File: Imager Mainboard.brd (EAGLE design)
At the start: 63.5 x 65 mm, 45 parts, among them IC1 7805H, IC2 MAX3490, IC3 SC16IS740IPW, IC4 MAX3490, IC6 AD7714R-24, J1 RASPBERRYPI-40-PIN-GPIO_PTH_N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, J14 U.FL, Q1 ASFL1, Q2 1.8432 MHz

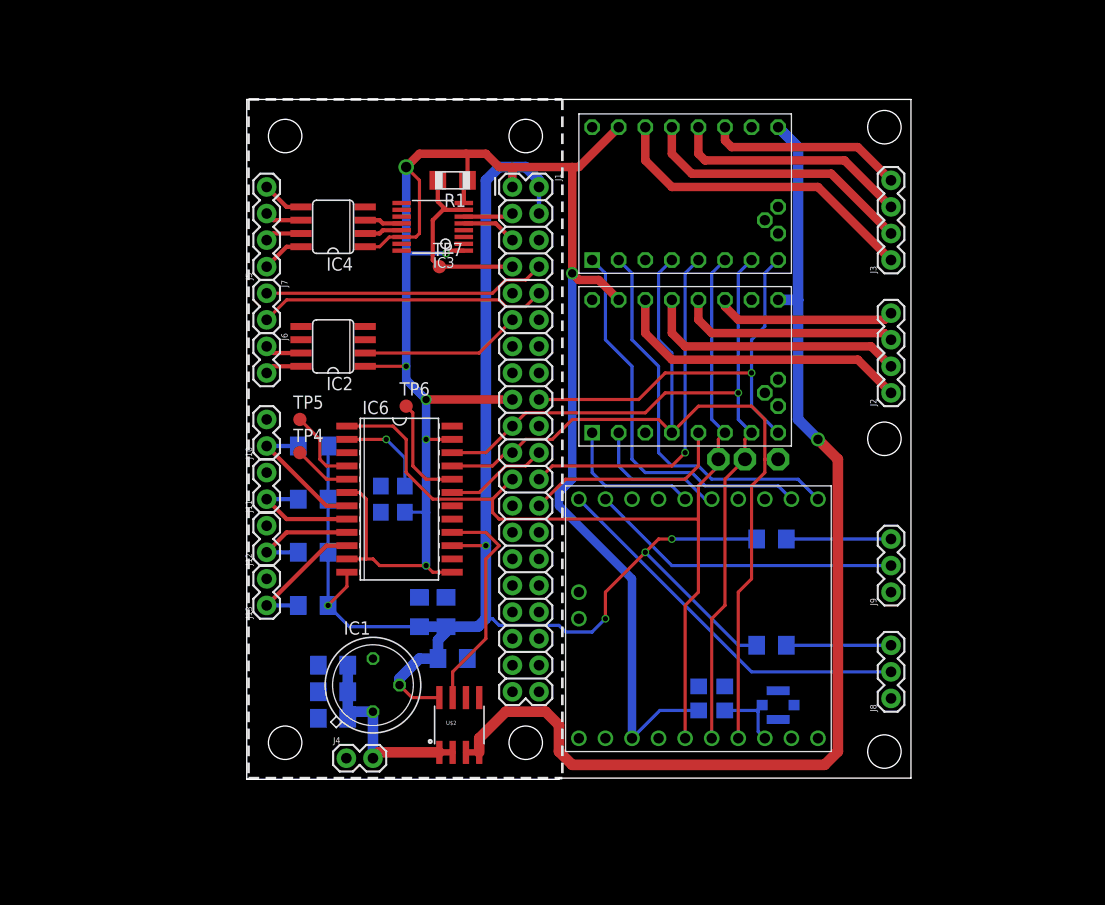
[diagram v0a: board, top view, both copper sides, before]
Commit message: Adding test pads
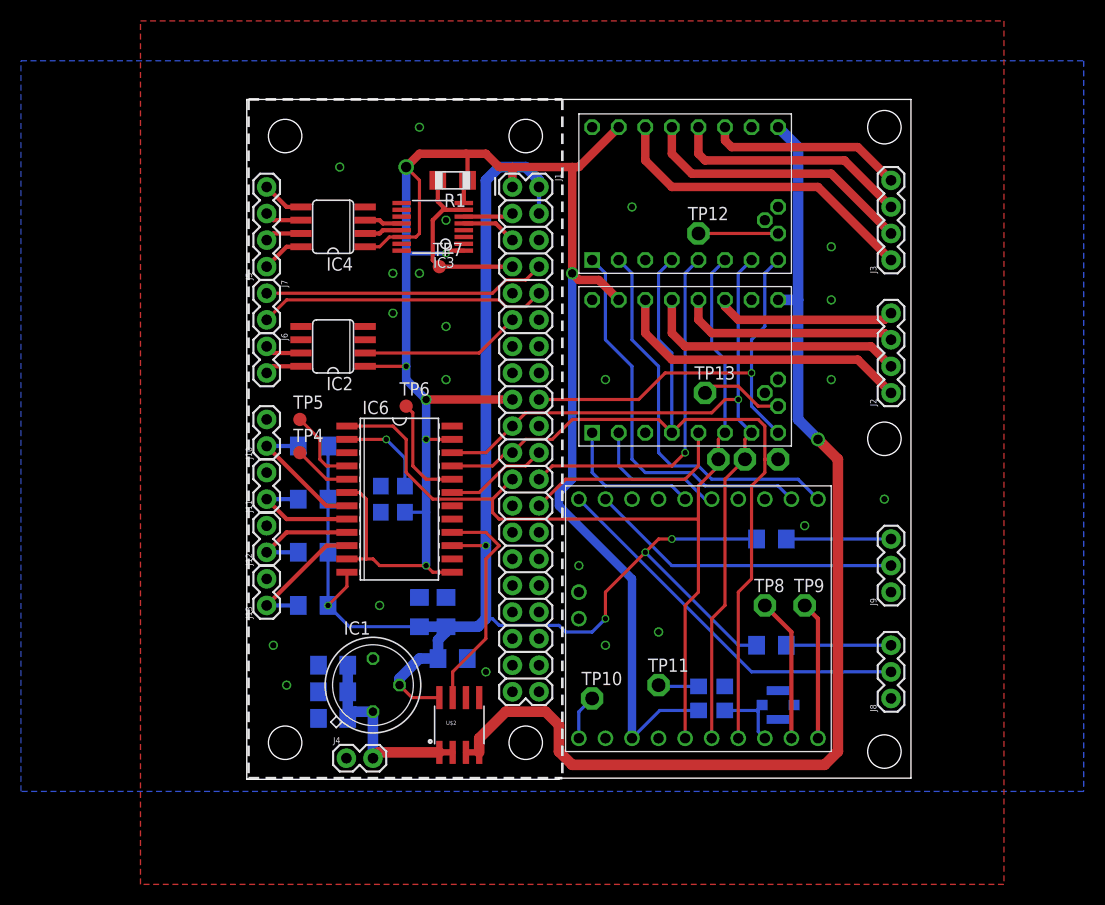
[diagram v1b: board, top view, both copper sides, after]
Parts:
- added TP10, TP11, TP12, TP13, TP8, TP9: PTR1PAD1-13, testpad:P1-13
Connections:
- new net N$21: TP8.TP, U$1.P$9
- new net N$25: TP9.TP, U$1.P$10
- new net N$26: TP10.TP, U$1.P$1
- new net N$27: Q1.1, TP11.TP
- new net N$28: DRV2.P$17, TP12.TP
- new net N$29: DRV1.P$17, TP13.TP
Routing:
- net N$21: track 0.00 -> 13.8 mm
- net N$25: track 0.00 -> 13.2 mm
- net N$29: track 0.00 -> 8.04 mm
- net N$28: track 0.00 -> 7.62 mm
- net N$26: track 0.00 -> 4.34 mm
- net N$27: track 0.00 -> 3.88 mm
- net MISO: track 84.2 -> 82.8 mm
- net +5V: track 148.2 -> 148.7 mm
- added copper zone on layer 1, net GND
- added copper zone on layer 16, net GND

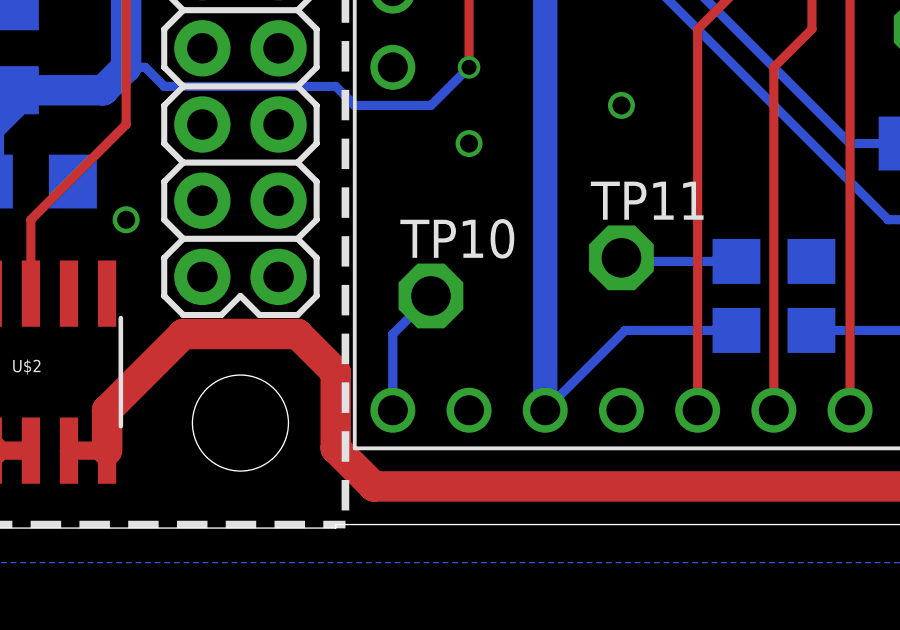
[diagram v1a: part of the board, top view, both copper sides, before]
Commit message: Adding TMC429 CS
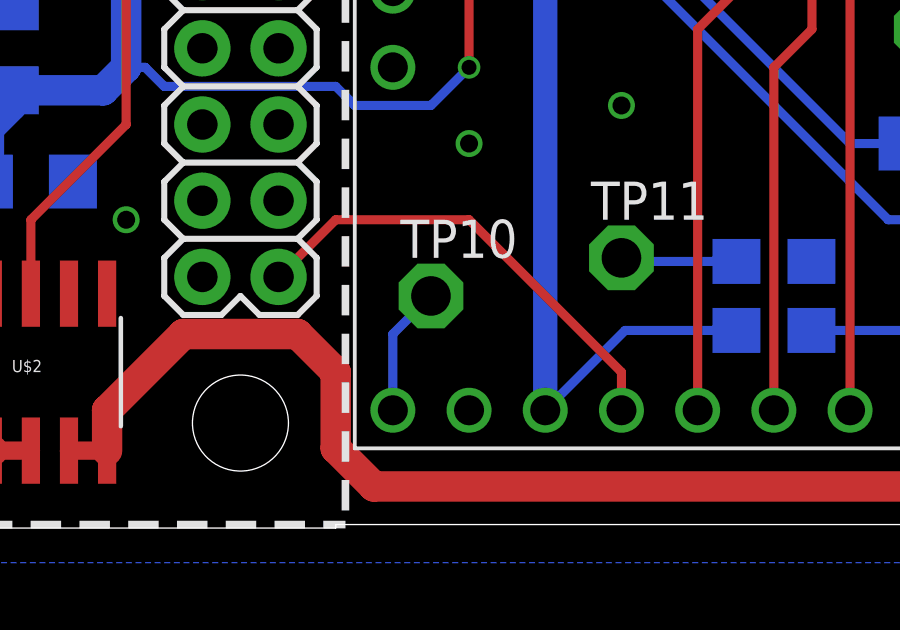
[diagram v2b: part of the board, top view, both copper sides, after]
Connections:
- removed net N$31: U$1.P$4
- new net CS3: J1.40, U$1.P$4
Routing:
- net CS3: track 0.00 -> 15.6 mm
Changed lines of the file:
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@@
 <wire x1="51.587" y1="22.86" x2="61.595" y2="22.86" width="0.3048" layer="16"/>
 </signal>
-<signal name="N$31">
+<signal name="CS3">
 <contactref element="U$1" pad="P$4"/>
+<contactref element="J1" pad="40"/>
+<wire x1="39.37" y1="3.81" x2="39.37" y2="5.08" width="0.3048" layer="1"/>
+<wire x1="39.37" y1="5.08" x2="34.29" y2="10.16" width="0.3048" layer="1"/>
+<wire x1="34.29" y1="10.16" x2="29.845" y2="10.16" width="0.3048" layer="1"/>
+<wire x1="29.845" y1="10.16" x2="27.94" y2="8.255" width="0.3048" layer="1"/>
 </signal>
 <signal name="VMOT">

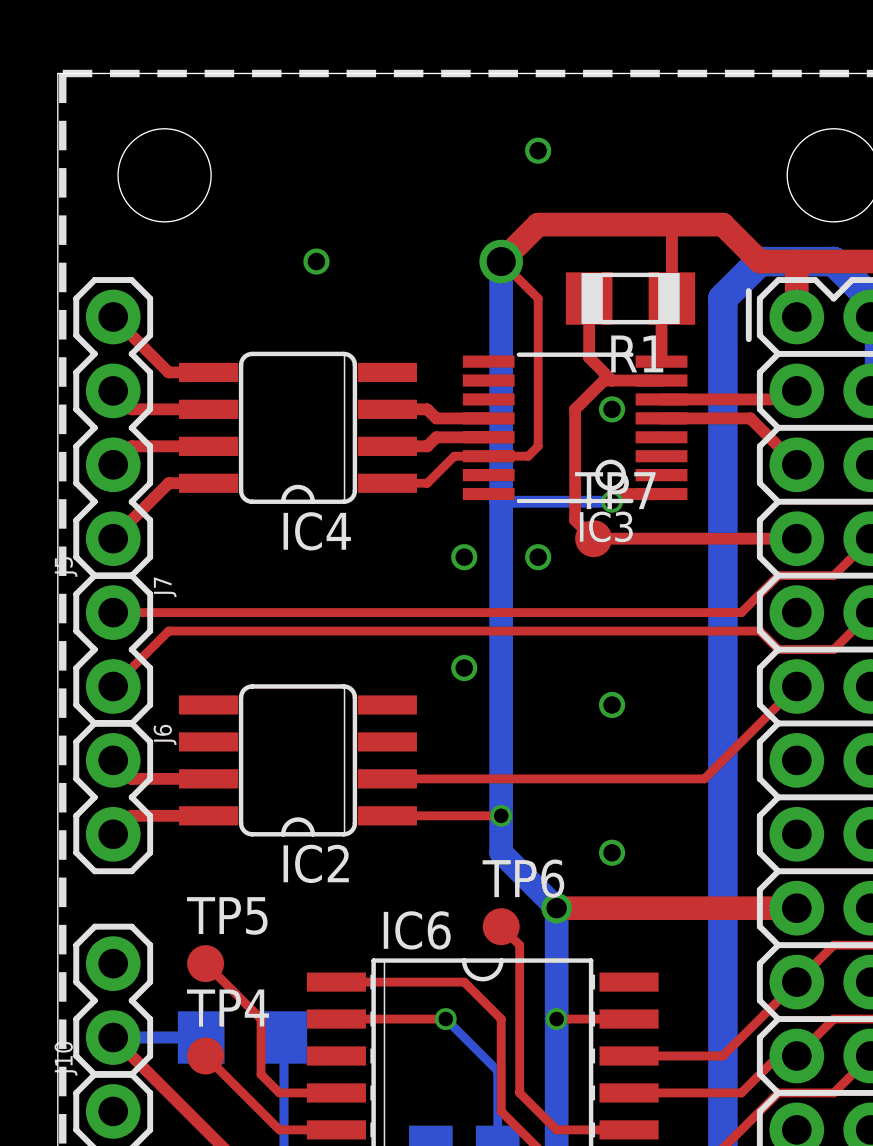
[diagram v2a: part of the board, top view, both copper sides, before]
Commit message: Adding serial test points
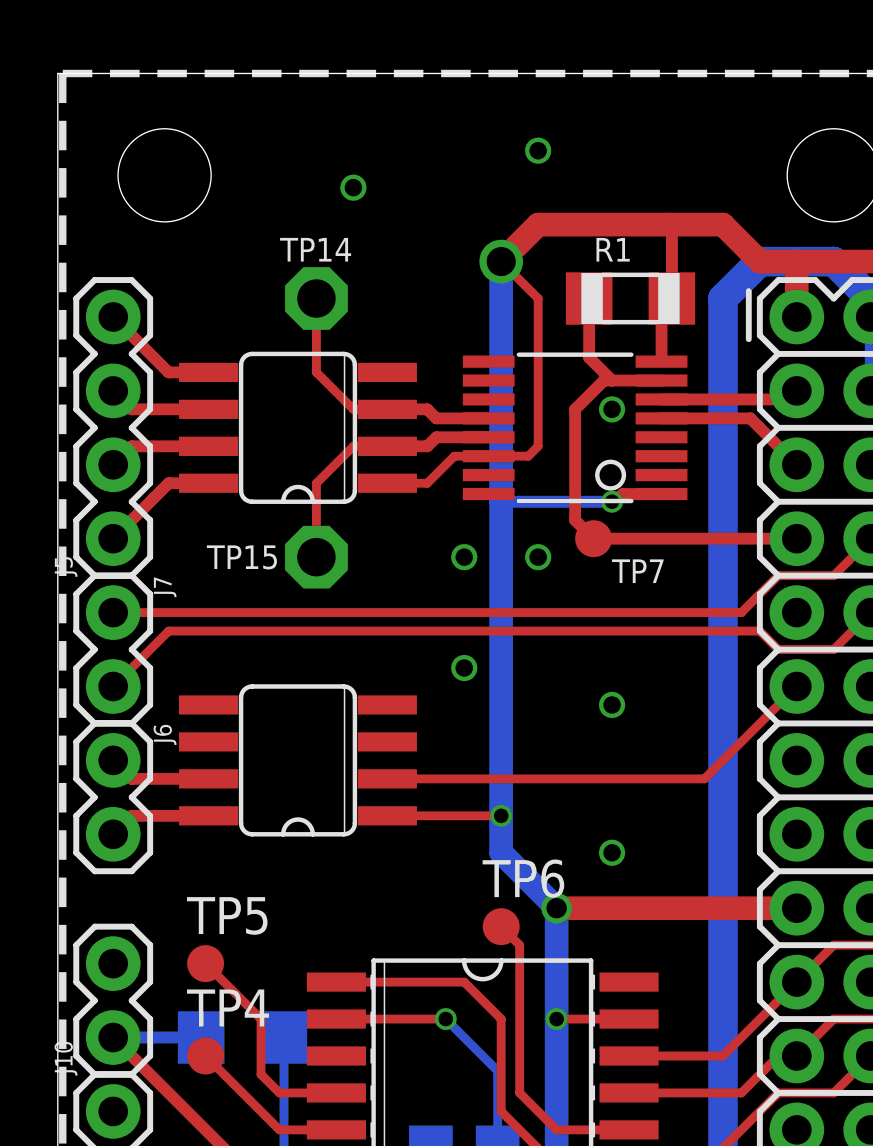
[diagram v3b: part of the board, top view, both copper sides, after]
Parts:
- added TP14, TP15: PTR1PAD1-13, testpad:P1-13
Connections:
- net N$3: now also TP14.TP
- net N$37: now also TP15.TP
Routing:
- net N$37: track 3.61 -> 9.11 mm
- net N$3: track 3.61 -> 9.11 mm
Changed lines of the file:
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@@
 <attribute name="PROD_ID" value="CONN-09696" x="1.905" y="48.895" size="1.778" layer="27" rot="R90" display="off"/>
 </element>
-<element name="IC4" library="maxim" package="SO08" value="MAX3490" x="8.255" y="52.705" rot="R90">
+<element name="IC4" library="maxim" package="SO08" value="MAX3490" x="8.255" y="52.705" smashed="yes" rot="R90">
 <attribute name="MF" value="" x="8.255" y="52.705" size="1.778" layer="27" rot="R90" display="off"/>
 <attribute name="OC_NEWARK" value="unknown" x="8.255" y="52.705" size="1.778" layer="27" rot="R90" display="off"/>
@@
 <attribute name="MPN" value="" x="8.255" y="52.705" size="1.778" layer="27" rot="R90" display="off"/>
 </element>
-<element name="IC2" library="maxim" package="SO08" value="MAX3490" x="8.255" y="41.275" rot="R90">
+<element name="IC2" library="maxim" package="SO08" value="MAX3490" x="8.255" y="41.275" smashed="yes" rot="R90">
 <attribute name="MF" value="" x="8.255" y="41.275" size="1.778" layer="27" rot="R90" display="off"/>
 <attribute name="OC_NEWARK" value="unknown" x="8.255" y="41.275" size="1.778" layer="27" rot="R90" display="off"/>
@@
 </element>
 <element name="J6" library="SparkFun-Connectors" package="1X02" value="" x="1.905" y="41.275" rot="R270"/>
-<element name="IC3" library="FRC696" package="TSSOP16L" value="SC16IS740IPW" x="17.78" y="52.705" rot="R90"/>
+<element name="IC3" library="FRC696" package="TSSOP16L" value="SC16IS740IPW" x="17.78" y="52.705" smashed="yes" rot="R90"/>
 <element name="DRV2" library="FRC696" package="SILENTSTEPSTICK" value="SILENTSTEPSTICK" x="40.64" y="55.88" rot="R90"/>
 <element name="DRV1" library="FRC696" package="SILENTSTEPSTICK" value="SILENTSTEPSTICK" x="40.64" y="39.37" rot="R90"/>
 <element name="J7" library="SparkFun-Connectors" package="1X02" value="" x="1.905" y="46.355" rot="R270"/>
-<element name="R1" library="resistor" package="R1206" value="" x="19.685" y="57.15" rot="R180"/>
+<element name="R1" library="resistor" package="R1206" value="" x="19.685" y="57.15" smashed="yes" rot="R180">
+<attribute name="NAME" x="18.415" y="58.42" size="0.8128" layer="25" font="fixed"/>
+<attribute name="VALUE" x="20.955" y="59.69" size="1.27" layer="27" rot="R180"/>
+</element>
 <element name="R2" library="resistor" package="R1206" value="" x="50.165" y="12.7" rot="MR180"/>
 <element name="R3" library="resistor" package="R1206" value="" x="50.165" y="22.86" rot="MR180"/>
@@
 <element name="J12" library="SparkFun-Connectors" package="1X02" value="" x="1.905" y="21.59" rot="R90"/>
 <element name="J13" library="SparkFun-Connectors" package="1X02" value="" x="1.905" y="16.51" rot="R90"/>
-<element name="IC6" library="analog-devices" package="SO24R" value="AD7714R-24" x="14.605" y="26.67" rot="R270">
+<element name="IC6" library="analog-devices" package="SO24R" value="AD7714R-24" x="14.605" y="26.67" smashed="yes" rot="R270">
 <attribute name="OC_FARNELL" value="unknown" x="14.605" y="26.67" size="1.778" layer="27" rot="R270" display="off"/>
 <attribute name="MPN" value="" x="14.605" y="26.67" size="1.778" layer="27" rot="R270" display="off"/>
@@
 <attribute name="PROD_ID" value="CONN-09193" x="50.8" y="6.985" size="1.778" layer="28" rot="MR0" display="off"/>
 </element>
-<element name="Q2" library="crystal" package="ASF" value="1.8432 MHz" x="13.97" y="26.67" rot="MR90">
+<element name="Q2" library="crystal" package="ASF" value="1.8432 MHz" x="13.97" y="26.67" smashed="yes" rot="MR90">
 <attribute name="MPN" value="ASFL1-125.000MHZ-EC-T" x="13.97" y="26.67" size="1.778" layer="28" rot="MR90" display="off"/>
 <attribute name="MF" value="Abracon Corporation" x="13.97" y="26.67" size="1.778" layer="28" rot="MR90" display="off"/>
 <attribute name="OC_NEWARK" value="19M1882" x="13.97" y="26.67" size="1.778" layer="28" rot="MR90" display="off"/>
 <attribute name="OC_FARNELL" value="1838931" x="13.97" y="26.67" size="1.778" layer="28" rot="MR90" display="off"/>
+<attribute name="NAME" x="16.51" y="24.13" size="1.27" layer="26" rot="MR90"/>
+<attribute name="VALUE" x="10.16" y="24.13" size="1.27" layer="28" rot="MR90"/>
 </element>
 <element name="TP4" library="testpad" package="B1,27" value="PTR1B1,27" x="5.08" y="31.115">
@@
 <attribute name="TP_SIGNAL_NAME" value="" x="15.24" y="35.56" size="1.778" layer="27" display="off"/>
 </element>
-<element name="TP7" library="testpad" package="B1,27" value="PTR1B1,27" x="18.415" y="48.895">
-<attribute name="TP_SIGNAL_NAME" value="" x="18.415" y="48.895" size="1.778" layer="27" display="off"/>
+<element name="TP7" library="testpad" package="B1,27" value="PTR1B1,27" x="18.415" y="48.895" smashed="yes">
+<attribute name="TP_SIGNAL_NAME" value="" x="17.78" y="46.99" size="1" layer="37"/>
+<attribute name="NAME" x="19.05" y="47.371" size="0.8128" layer="25" font="fixed" ratio="10"/>
 </element>
 <element name="TP8" library="testpad" package="P1-13" value="PTR1PAD1-13" x="49.53" y="16.51">
@@
 <element name="TP13" library="testpad" package="P1-13" value="PTR1PAD1-13" x="43.815" y="36.83">
 <attribute name="TP_SIGNAL_NAME" value="" x="43.815" y="36.83" size="1.778" layer="27" display="off"/>
+</element>
+<element name="TP14" library="testpad" package="P1-13" value="PTR1PAD1-13" x="8.89" y="57.15" smashed="yes">
+<attribute name="TP_SIGNAL_NAME" value="" x="7.62" y="54.61" size="1" layer="37"/>
+<attribute name="NAME" x="8.89" y="58.42" size="0.8128" layer="25" font="fixed" ratio="10" align="bottom-center"/>
+</element>
+<element name="TP15" library="testpad" package="P1-13" value="PTR1PAD1-13" x="8.89" y="48.26" smashed="yes">
+<attribute name="TP_SIGNAL_NAME" value="" x="7.62" y="45.72" size="1" layer="37"/>
+<attribute name="NAME" x="7.62" y="48.26" size="0.8128" layer="25" font="fixed" ratio="10" align="center-right"/>
 </element>
 </elements>
@@
 <via x="16.51" y="48.26" extent="1-16" drill="0.6"/>
 <via x="13.97" y="48.26" extent="1-16" drill="0.6"/>
-<via x="8.89" y="58.42" extent="1-16" drill="0.6"/>
+<via x="10.16" y="60.96" extent="1-16" drill="0.6"/>
 <via x="16.51" y="62.23" extent="1-16" drill="0.6"/>
 <via x="13.97" y="44.45" extent="1-16" drill="0.6"/>
@@
 <wire x1="13.01" y1="53.03" x2="12.7" y2="53.34" width="0.4064" layer="1"/>
 <wire x1="12.7" y1="53.34" x2="11.3284" y2="53.34" width="0.4064" layer="1"/>
+<contactref element="TP14" pad="TP"/>
+<wire x1="11.3284" y1="53.34" x2="10.16" y2="53.34" width="0.3048" layer="1"/>
+<wire x1="10.16" y1="53.34" x2="8.89" y2="54.61" width="0.3048" layer="1"/>
+<wire x1="8.89" y1="54.61" x2="8.89" y2="57.15" width="0.3048" layer="1"/>
 </signal>
 <signal name="N$37">
@@
 <wire x1="13.01" y1="52.38" x2="12.7" y2="52.07" width="0.4064" layer="1"/>
 <wire x1="12.7" y1="52.07" x2="11.3284" y2="52.07" width="0.4064" layer="1"/>
+<contactref element="TP15" pad="TP"/>
+<wire x1="11.3284" y1="52.07" x2="10.16" y2="52.07" width="0.3048" layer="1"/>
+<wire x1="10.16" y1="52.07" x2="8.89" y2="50.8" width="0.3048" layer="1"/>
+<wire x1="8.89" y1="50.8" x2="8.89" y2="48.26" width="0.3048" layer="1"/>
 </signal>
 <signal name="SCL">

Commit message: Adding SC16IS740 oscillator section and limit switch pullups
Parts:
- added C1, C2: 18 pF, resistor:C1206
- added Q3: (no value), SparkFun-Clocks:CRYSTAL-SMD-5X3.2-4PAD
- added R10, R9: (no value), resistor:R1206
- added R8: 1M, resistor:R1206
- added TP16, TP17: PTR1PAD1-13, testpad:P1-13
- moved DRV1 16.5 mm to (40.6, 55.9)
- moved DRV2 16.5 mm to (40.6, 39.4)
- moved TP15 9.86 mm to (6.35, 57.8)
- moved TP7 3.18 mm to (21.6, 48.9)
- moved IC4 0.64 mm to (8.26, 53.3)
- moved IC2 0.63 mm to (8.26, 40.6)
- moved J5 0.63 mm to (1.91, 49.5)
- moved J6 0.63 mm to (1.91, 40.6)
- moved TP14 0.63 mm to (8.89, 57.8)
- renumbered J2 to MOTOR2, J3 to MOTOR1, J8 to LIM1, J9 to LIM2, U$2 to U2
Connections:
- new net N$30: C2.1, IC3.15, Q3.3, R8.2
- new net N$31: C1.1, IC3.16, Q3.1, R8.1
- net +3V3: now also R10.1, R9.1
- net CS0: now also DRV1.P$5, TP17.TP; no longer DRV2.P$5
- net CS1: now also DRV2.P$5, TP16.TP; no longer DRV1.P$5
- net DIR1: now also DRV1.P$1; no longer DRV2.P$1
- net DIR2: now also DRV2.P$1; no longer DRV1.P$1
- net GND: now also C1.2, C2.2
- net LIM1: now also R9.2
- net LIM2: now also R10.2
- net N$1: now also DRV2.P$14; no longer DRV1.P$14
- net N$2: now also DRV2.P$13; no longer DRV1.P$13
- net N$28: now also DRV1.P$17; no longer DRV2.P$17
- net N$29: now also DRV2.P$17; no longer DRV1.P$17
- net N$4: now also DRV2.P$12; no longer DRV1.P$12
- net N$5: now also DRV2.P$11; no longer DRV1.P$11
- net N$6: now also DRV1.P$14; no longer DRV2.P$14
- net N$7: now also DRV1.P$13; no longer DRV2.P$13
- net N$8: now also DRV1.P$12; no longer DRV2.P$12
- net N$9: now also DRV1.P$11; no longer DRV2.P$11
- net STEP1: now also DRV1.P$2; no longer DRV2.P$2
- net STEP2: now also DRV2.P$2; no longer DRV1.P$2
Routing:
- net N$30: track 0.00 -> 13.0 mm
- net N$31: track 0.00 -> 12.1 mm
- net N$10: track 27.1 -> 31.7 mm, vias 0 -> 1
- net DIR2: track 13.8 -> 17.6 mm
- net +3V3: track 192.9 -> 196.6 mm
- net N$37: track 9.11 -> 12.2 mm
- net N$11: track 27.6 -> 29.9 mm, vias 0 -> 1
- net +5V: track 148.7 -> 147.1 mm
- net STEP2: track 13.4 -> 11.9 mm
- net LIM1: track 36.7 -> 38.0 mm
- net DIR1: track 37.4 -> 36.3 mm
- net N$3: track 9.11 -> 9.75 mm
- net LIM2: track 29.9 -> 30.5 mm
